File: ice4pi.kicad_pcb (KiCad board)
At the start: 4 copper layers, 65 x 30 mm, 61 parts, among them J1 Pmod 2x6, J2 Raspberry_Pi_2_3, U1 ICE40HX1K-TQ144, U2 W25Q32JVSSIQ, U3 LT3030, U4 DSC1001DI1-012.0000

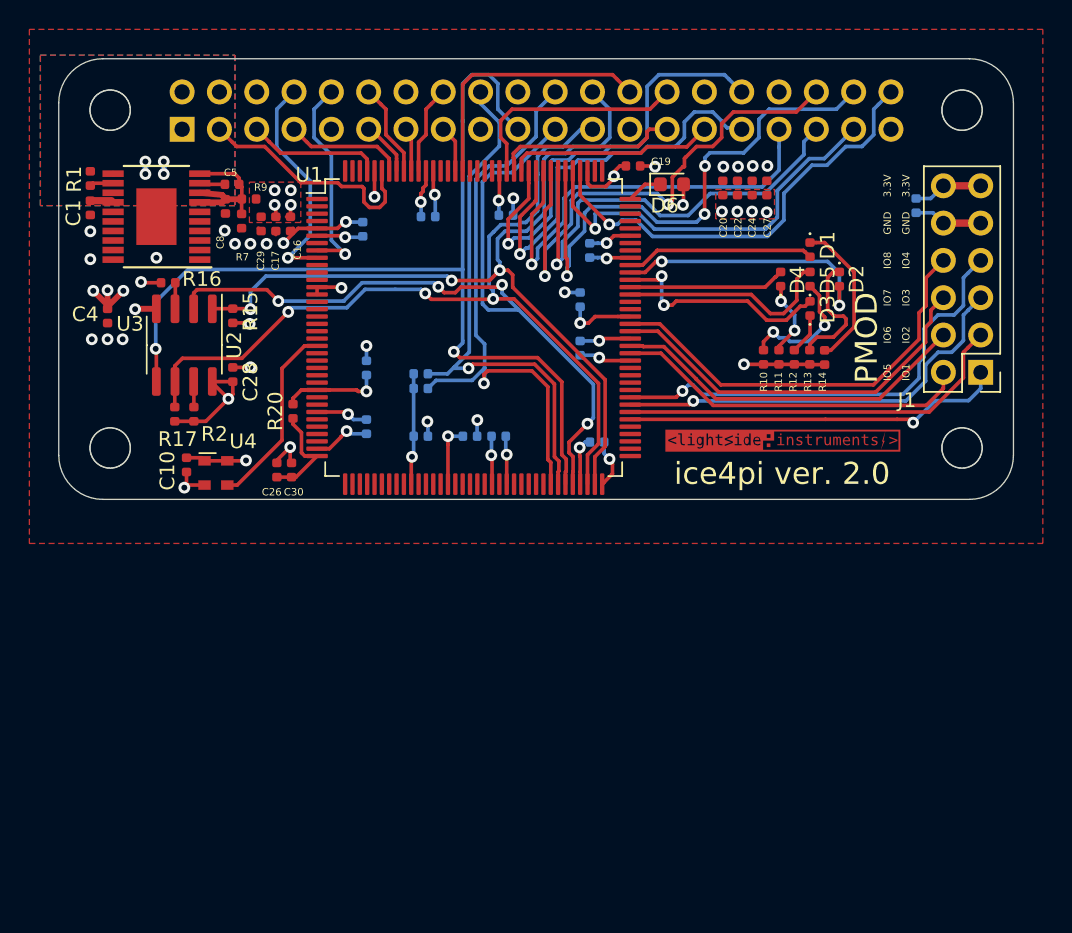
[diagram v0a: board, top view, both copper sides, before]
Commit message: Release ice4pi-bridge-1.0
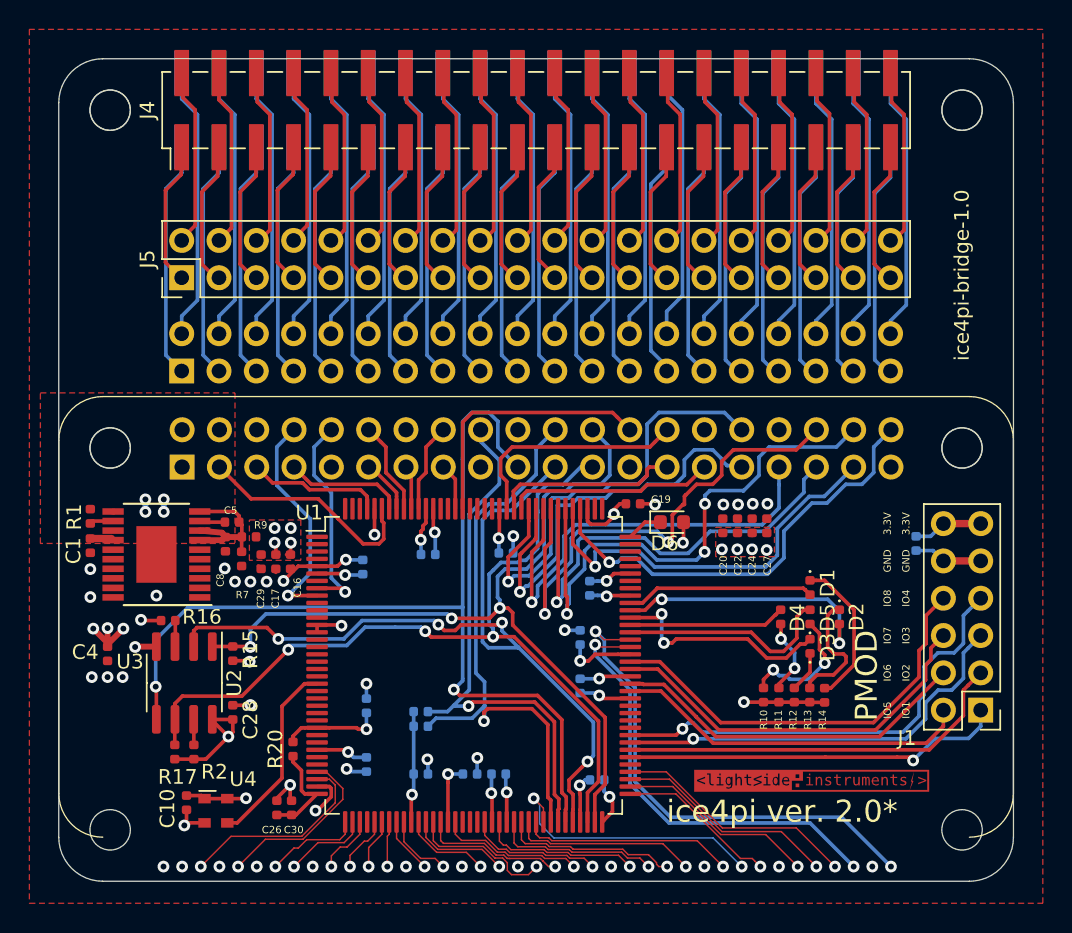
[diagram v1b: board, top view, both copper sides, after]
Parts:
- added ?: , ice4pi:mount_hole, F.Cu at (111.5, 101.5)
- added ?: , ice4pi:mount_hole, F.Cu at (53.5, 101.5)
- added J3: raspberry_pi_2_3_4_ordered, Connector_PinSocket_2.54mm:PinSocket_2x20_P2.54mm_Vertical_SMD, B.Cu at (82.5, 52.5)
- added J4: raspberry_pi_2_3_4_ordered, Connector_PinHeader_2.54mm:PinHeader_2x20_P2.54mm_Vertical_SMD, F.Cu at (82.5, 52.5)
- added J5: raspberry_pi_2_3_4_ordered, Connector_PinHeader_2.54mm:PinHeader_2x20_P2.54mm_Vertical, F.Cu at (58.4, 63.9)
- added J6: raspberry_pi_2_3_4_ordered, Connector_PinSocket_2.54mm:PinSocket_2x20_P2.54mm_Vertical, B.Cu at (58.4, 70.3)
- J2: value Raspberry_Pi_2_3 -> raspberry_pi_2_3_4_ordered
- moved svg2mod 23.2 mm to (101.3, 98.7)
- moved C1 23.0 mm to (52.1, 82.2)
- moved C6 23.0 mm to (80.5, 82.7)
- moved R1 23.0 mm to (52.1, 80.2)
- moved C10 23.0 mm to (58.7, 99.7)
- moved C11 23.0 mm to (85.5, 91.7)
- moved C12 23.0 mm to (74.7, 97.7)
- moved C13 23.0 mm to (80.0, 97.7)
- moved C14 23.0 mm to (71.0, 97.0)
- moved C15 23.0 mm to (70.7, 83.6)
- moved C16 23.0 mm to (65.8, 83.2)
- moved C17 23.0 mm to (64.8, 83.2)
- moved C18 23.0 mm to (86.7, 98.1)
- moved C19 23.0 mm to (89.1, 79.3)
- moved C2 23.0 mm to (108.4, 82.0)
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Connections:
- net +3V3 renamed PIEXT1
- net +5V renamed PIEXT2
- net GND renamed PIEXT14
- U1 pad 1: (no net) -> Net-(U1-Pad1)
- U1 pad 10: (no net) -> Net-(U1-Pad10)
- U1 pad 101: (no net) -> Net-(U1-Pad101)
- U1 pad 102: (no net) -> Net-(U1-Pad102)
- U1 pad 104: (no net) -> Net-(U1-Pad104)
- U1 pad 105: (no net) -> IR_TXD
- U1 pad 106: (no net) -> IR_RXD
- U1 pad 107: (no net) -> IR_SD
- U1 pad 109: (no net) -> Net-(U1-Pad109)
- U1 pad 11: (no net) -> Net-(U1-Pad11)
- U1 pad 110: (no net) -> Net-(U1-Pad110)
- U1 pad 12: (no net) -> Net-(U1-Pad12)
- U1 pad 124: (no net) -> Net-(U1-Pad124)
- U1 pad 125: (no net) -> Net-(U1-Pad125)
- U1 pad 126: (no net) -> Net-(U1-Pad126)
- U1 pad 127: (no net) -> Net-(U1-Pad127)
- U1 pad 130: (no net) -> Net-(U1-Pad130)
- U1 pad 131: (no net) -> Net-(U1-Pad131)
- U1 pad 142: (no net) -> Net-(U1-Pad142)
- U1 pad 143: (no net) -> Net-(U1-Pad143)
- U1 pad 144: (no net) -> Net-(U1-Pad144)
- U1 pad 15: (no net) -> Net-(U1-Pad15)
- U1 pad 16: (no net) -> Net-(U1-Pad16)
- U1 pad 17: (no net) -> Net-(U1-Pad17)
- U1 pad 18: (no net) -> Net-(U1-Pad18)
- U1 pad 19: (no net) -> Net-(U1-Pad19)
- U1 pad 2: (no net) -> Net-(U1-Pad2)
- U1 pad 20: (no net) -> Net-(U1-Pad20)
- U1 pad 22: (no net) -> Net-(U1-Pad22)
- U1 pad 23: (no net) -> Net-(U1-Pad23)
- U1 pad 24: (no net) -> Net-(U1-Pad24)
- U1 pad 25: (no net) -> Net-(U1-Pad25)
- U1 pad 26: (no net) -> Net-(U1-Pad26)
- U1 pad 28: (no net) -> Net-(U1-Pad28)
- U1 pad 29: (no net) -> Net-(U1-Pad29)
- U1 pad 3: (no net) -> Net-(U1-Pad3)
- U1 pad 31: (no net) -> Net-(U1-Pad31)
- U1 pad 32: (no net) -> Net-(U1-Pad32)
- U1 pad 33: (no net) -> PIEXT5
- U1 pad 34: (no net) -> PIEXT3
- U1 pad 37: (no net) -> PIEXT7
- U1 pad 38: (no net) -> PIEXT8
- U1 pad 39: (no net) -> PIEXT10
- U1 pad 4: (no net) -> Net-(U1-Pad4)
- U1 pad 40: (no net) -> Net-(U1-Pad40)
- U1 pad 41: (no net) -> PIEXT11
- U1 pad 42: (no net) -> PIEXT12
- U1 pad 43: (no net) -> PIEXT13
- U1 pad 44: (no net) -> PIEXT15
- U1 pad 45: (no net) -> PIEXT16
- U1 pad 47: (no net) -> PIEXT18
- U1 pad 48: (no net) -> PIEXT19
- U1 pad 49: (no net) -> PIEXT21
- U1 pad 50: (no net) -> PIEXT22
- U1 pad 52: (no net) -> PIEXT23
- U1 pad 53: (no net) -> Net-(U1-Pad53)
- U1 pad 54: (no net) -> Net-(U1-Pad54)
- U1 pad 55: (no net) -> Net-(U1-Pad55)
- U1 pad 56: (no net) -> PIEXT24
- U1 pad 58: (no net) -> PIEXT26
- U1 pad 60: (no net) -> PIEXT27
- U1 pad 61: (no net) -> PIEXT28
- U1 pad 62: (no net) -> PIEXT29
- U1 pad 63: (no net) -> PIEXT31
- U1 pad 64: (no net) -> PIEXT32
- U1 pad 7: (no net) -> Net-(U1-Pad7)
- U1 pad 73: (no net) -> PIEXT33
- U1 pad 74: (no net) -> PIEXT35
- U1 pad 75: (no net) -> PIEXT36
- U1 pad 76: (no net) -> PIEXT37
- U1 pad 77: (no net) -> Net-(U1-Pad77)
- U1 pad 82: (no net) -> Net-(U1-Pad82)
- U1 pad 83: (no net) -> Net-(U1-Pad83)
- U1 pad 84: (no net) -> Net-(U1-Pad84)
- U1 pad 85: (no net) -> Net-(U1-Pad85)
- U1 pad 93: (no net) -> PIEXT38
- U1 pad 94: (no net) -> PIEXT40
- U3 pad 1: (no net) -> Net-(U3-Pad1)
- U3 pad 17: (no net) -> Net-(U3-Pad17)
- U3 pad 18: (no net) -> Net-(U3-Pad18)
- U3 pad 19: (no net) -> Net-(U3-Pad19)
- U3 pad 2: (no net) -> Net-(U3-Pad2)
- U3 pad 3: (no net) -> Net-(U3-Pad3)
- U3 pad 4: (no net) -> Net-(U3-Pad4)
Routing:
- net PIEXT14: track 56.8 -> 698.4 mm, vias 35 -> 44
- net PIEXT2: track 4.36 -> 168.3 mm, vias 4 -> 6
- net PIEXT1: track 60.9 -> 211.5 mm, vias 21 -> 23
- net PIEXT40: track 0.00 -> 89.4 mm, vias 0 -> 2
- net PIEXT38: track 0.00 -> 86.1 mm, vias 0 -> 2
- net PIEXT32: track 0.00 -> 76.1 mm, vias 0 -> 2
- net PIEXT36: track 0.00 -> 70.8 mm, vias 0 -> 1
- net PIEXT28: track 0.00 -> 69.4 mm, vias 0 -> 1
- net PIEXT31: track 0.00 -> 69.2 mm, vias 0 -> 1
- net PIEXT22: track 0.00 -> 67.7 mm, vias 0 -> 1
- net PIEXT37: track 0.00 -> 67.3 mm, vias 0 -> 1
- net PIEXT26: track 0.00 -> 66.9 mm, vias 0 -> 1
- net PIEXT5: track 0.00 -> 65.8 mm, vias 0 -> 1
- net PIEXT24: track 0.00 -> 65.6 mm, vias 0 -> 1
- net PIEXT29: track 0.00 -> 65.2 mm, vias 0 -> 1
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- added copper zone on In1.Cu, net PIEXT2
- removed copper zone on B.Cu, net PIEXT2
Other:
- board size 65 x 30 mm -> 65 x 56 mm
- copper layers 4 -> 6
- net class Default: clearance 0.2 -> 0.1
- net class Thinest added: clearance 0.1, trace_width 0.1, via_dia 0.8, via_drill 0.4
- rule trace_clearance: 0.2 -> 0.1
- rule trace_min: 0.2 -> 0.1
- board text added: "ice4pi ver. 2.0*"
- board text added: "ice4pi-bridge-1.0"
- board text removed: "ice4pi ver. 2.0"
